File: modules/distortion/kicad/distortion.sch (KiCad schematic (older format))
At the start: 57 parts, among them P1 CONN_01X03, P10 CONN_01X03, P11 CONN_01X03, P12 CONN_01X03, P13 CONN_01X03, P14 CONN_01X03, P2 CONN_01X03, P3 CONN_01X03, P4 CONN_01X03, P5 CONN_01X03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

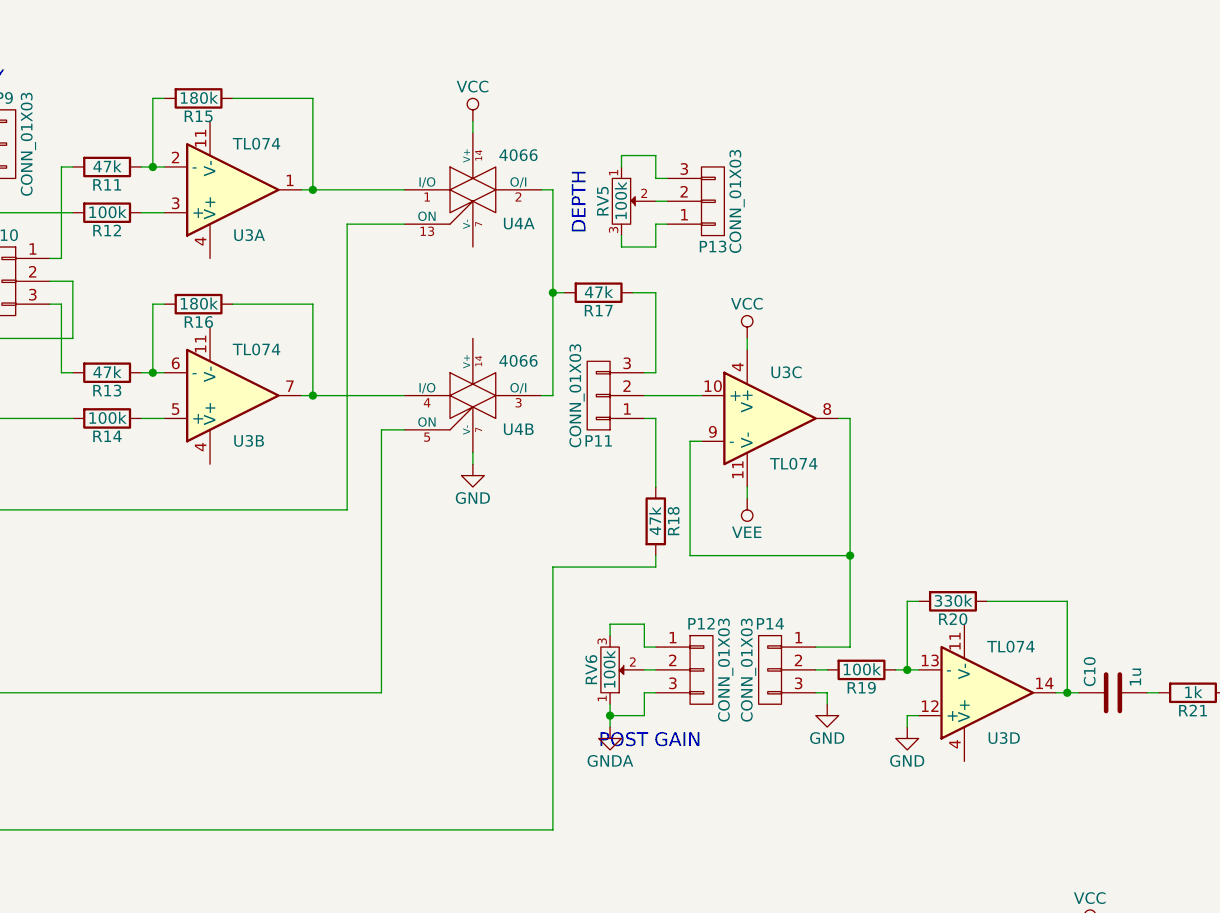
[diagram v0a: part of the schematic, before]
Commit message: Distortion pcb: panelization stuff, started layout wip
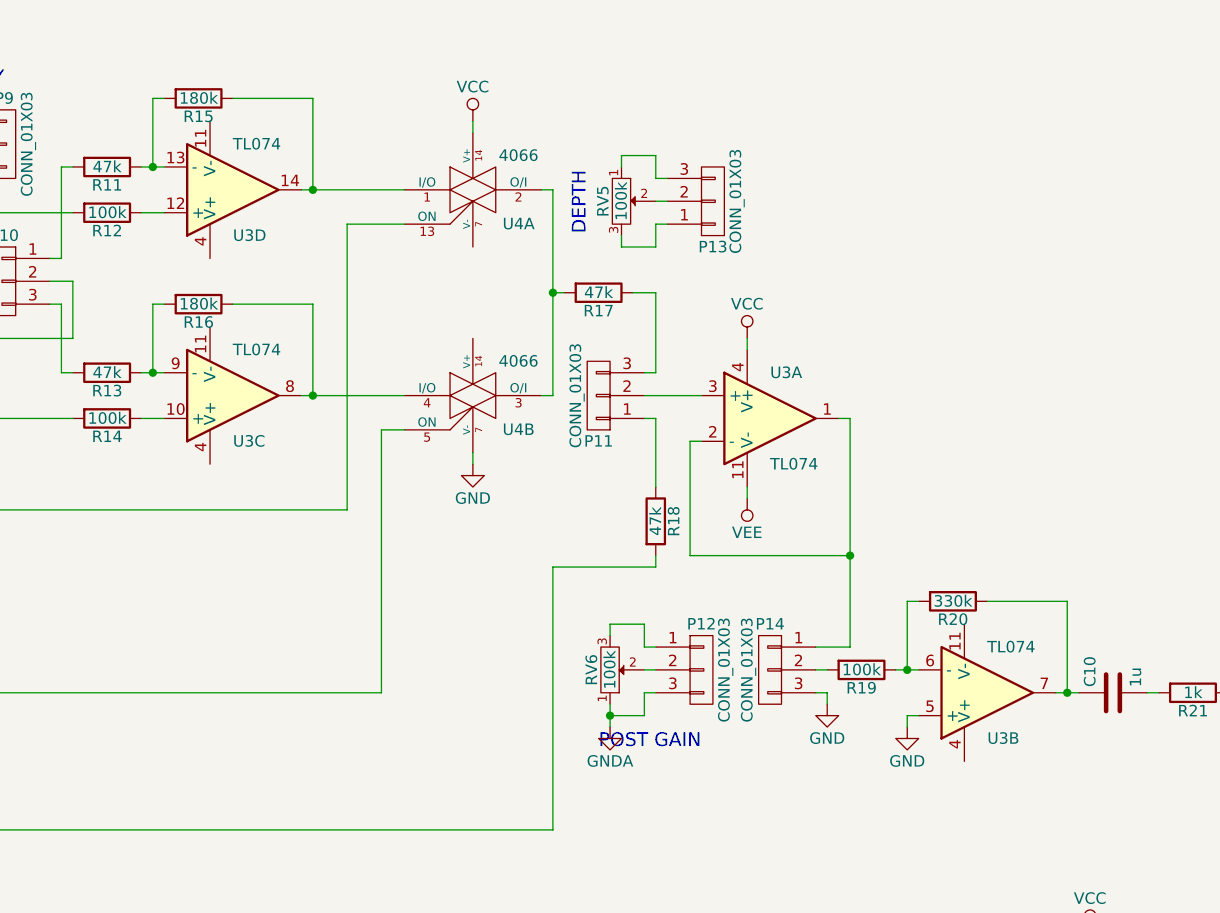
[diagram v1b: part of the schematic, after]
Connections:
- net GND: now also U3.5 (+); no longer U3.12 (+)
- net at R15.1, U4.1 (I/O): now also U3.14; no longer U3.1
- net at R11.1, R15.2: now also U3.13 (-); no longer U3.2 (-)
- net at R12.1: now also U3.12 (+); no longer U3.3 (+)
- net at P11.2 (P2): now also U3.3 (+); no longer U3.10 (+)
- net at R19.1, R20.2: now also U3.6 (-); no longer U3.13 (-)
- net at C10.1, R20.1: now also U3.7; no longer U3.14
- net at R14.1: now also U3.10 (+); no longer U3.5 (+)
- net at R13.1, R16.2: now also U3.9 (-); no longer U3.6 (-)
- net at R16.1, U4.4 (I/O): now also U3.8; no longer U3.7
- new net: P14.1 (P1), U3.1, U3.2 (-)
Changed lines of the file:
@@
 $Comp
 L TL074 U3
-U 1 1 597DDDFF
+U 4 1 597DDDFF
 P 5550 1400
 F 0 "U3" H 5550 1600 50  0000 L CNN
@@
 F 2 "Housings_DIP:DIP-14_W7.62mm_Socket_LongPads" H 5500 1500 50  0001 C CNN
 F 3 "" H 5600 1600 50  0000 C CNN
-	1    5550 1400
+	4    5550 1400
 	1    0    0    1
 $EndComp
 $Comp
 L TL074 U3
-U 3 1 597DDE8E
+U 1 1 597DDE8E
 P 7900 2400
 F 0 "U3" H 7900 2600 50  0000 L CNN
@@
 F 2 "Housings_DIP:DIP-14_W7.62mm_Socket_LongPads" H 7850 2500 50  0001 C CNN
 F 3 "" H 7950 2600 50  0000 C CNN
-	3    7900 2400
+	1    7900 2400
 	1    0    0    -1
 $EndComp
 $Comp
 L TL074 U3
-U 4 1 597DDEF7
+U 2 1 597DDEF7
 P 8850 3600
 F 0 "U3" H 8850 3800 50  0000 L CNN
@@
 F 2 "Housings_DIP:DIP-14_W7.62mm_Socket_LongPads" H 8800 3700 50  0001 C CNN
 F 3 "" H 8900 3800 50  0000 C CNN
-	4    8850 3600
+	2    8850 3600
 	1    0    0    1
 $EndComp
 $Comp
 L TL074 U3
-U 2 1 597DDF56
+U 3 1 597DDF56
 P 5550 2300
 F 0 "U3" H 5550 2500 50  0000 L CNN
@@
 F 2 "Housings_DIP:DIP-14_W7.62mm_Socket_LongPads" H 5500 2400 50  0001 C CNN
 F 3 "" H 5600 2500 50  0000 C CNN
-	2    5550 2300
+	3    5550 2300
 	1    0    0    1
 $EndComp
@@
 Connection ~ 7200 3700
 $Comp
-L GNDA #PWR?
+L GNDA #PWR032
 U 1 1 59875892
 P 3000 5650
-F 0 "#PWR?" H 3000 5400 50  0001 C CNN
+F 0 "#PWR032" H 3000 5400 50  0001 C CNN
 F 1 "GNDA" H 3000 5500 50  0000 C CNN
 F 2 "" H 3000 5650 50  0000 C CNN
@@
 $EndComp
 $Comp
-L PWR_FLAG #FLG?
+L PWR_FLAG #FLG033
 U 1 1 59876034
 P 3000 5600
-F 0 "#FLG?" H 3000 5695 50  0001 C CNN
+F 0 "#FLG033" H 3000 5695 50  0001 C CNN
 F 1 "PWR_FLAG" H 3000 5780 50  0000 C CNN
 F 2 "" H 3000 5600 50  0000 C CNN

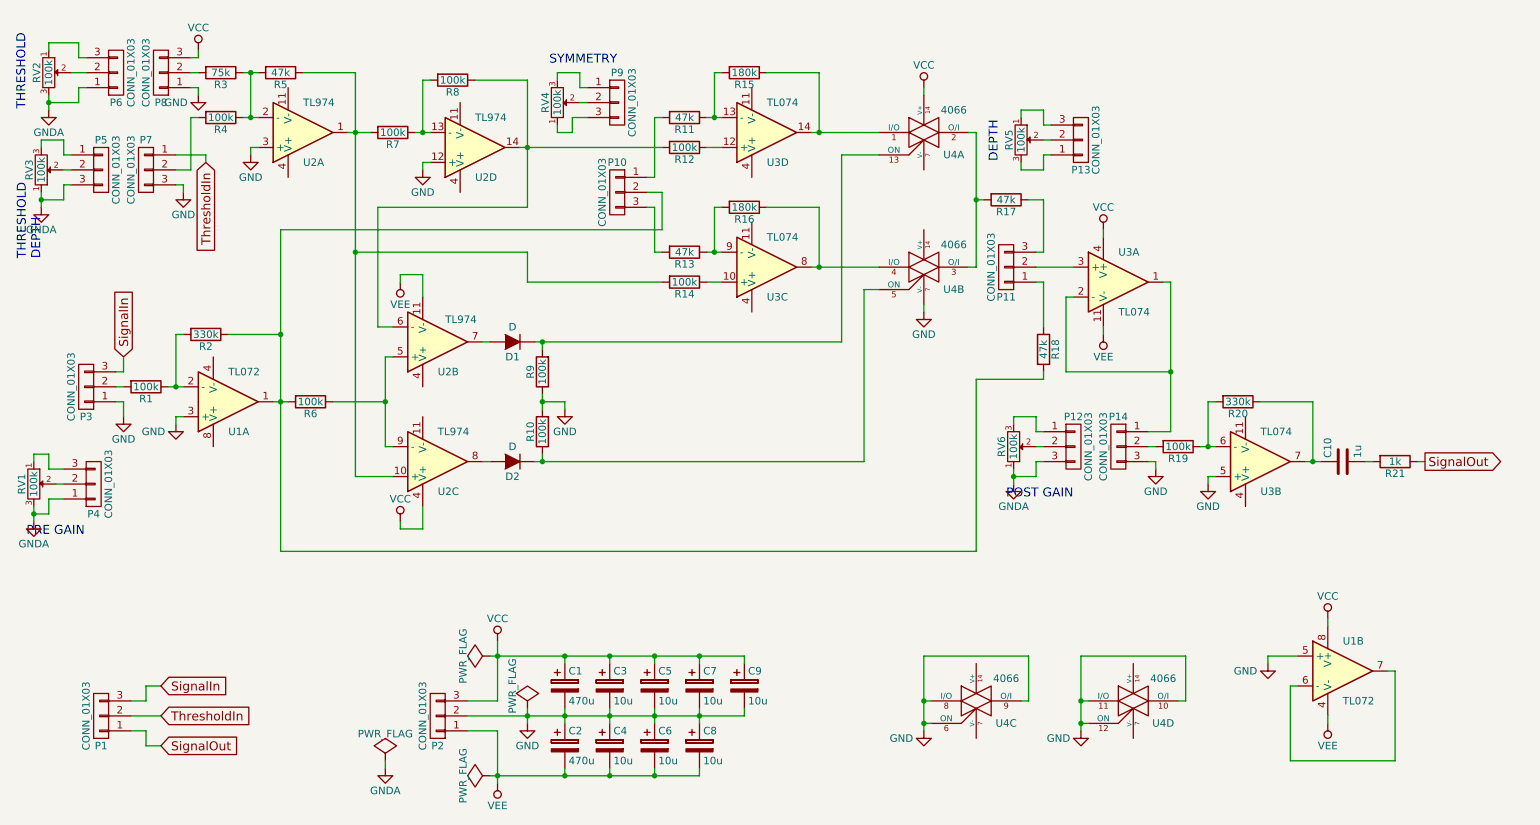
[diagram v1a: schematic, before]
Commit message: Distortion: move some resistors to top board WIP
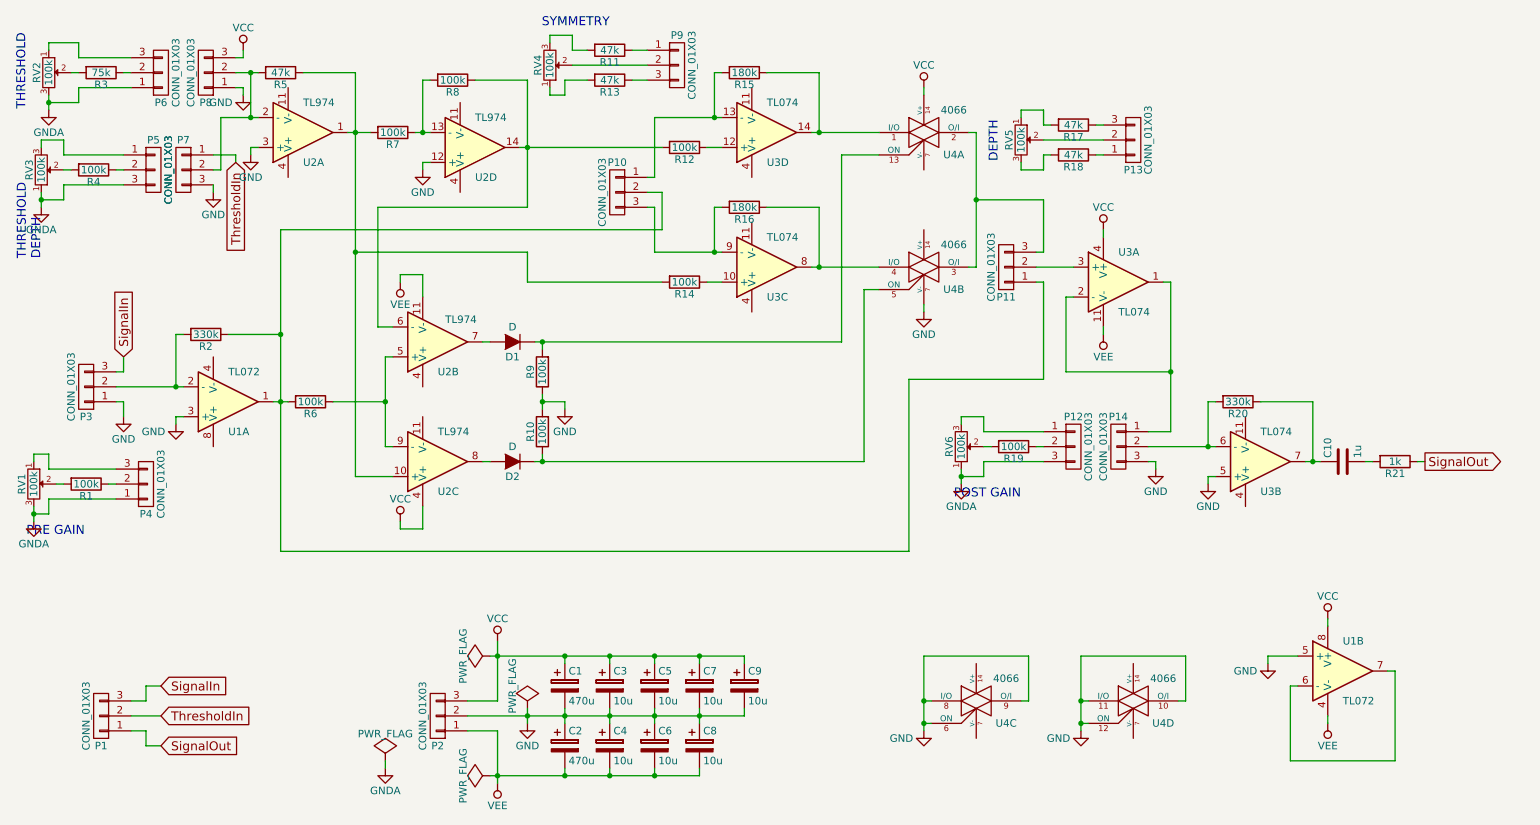
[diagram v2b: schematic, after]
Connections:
- net at R5.2, U2.2 (-): now also P7.2 (P2), P8.2 (P2); no longer R3.1, R4.1
- net at R15.2, U3.13 (-): now also P10.1 (P1); no longer R11.1
- net at R20.2, U3.6 (-): now also P14.2 (P2); no longer R19.1
- net at R16.2, U3.9 (-): now also P10.3 (P3); no longer R13.1
- net at U4.2 (O/I), U4.3 (O/I): now also P11.3 (P3); no longer R17.2
- net at RV2.2: now also R3.2; no longer P6.2 (P2)
- net at R4.2: now also RV3.2; no longer P7.2 (P2)
- net at P5.2 (P2): now also R4.1; no longer RV3.2
- net at P10.2 (P2), R2.1, R6.2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: now also P11.1 (P1); no longer R18.2
- net at R11.2: now also RV4.3; no longer P10.1 (P1)
- net at R13.2: now also RV4.1; no longer P10.3 (P3)
- net at P9.3 (P3): now also R13.1; no longer RV4.1
- net at P9.1 (P1): now also R11.1; no longer RV4.3
- net at R17.1: now also P13.3 (P3); no longer P11.3 (P3)
- net at R18.1: now also P13.1 (P1); no longer P11.1 (P1)
- net at RV5.1: now also R17.2; no longer P13.3 (P3)
- net at RV5.3: now also R18.2; no longer P13.1 (P1)
- net at RV6.2: now also R19.2; no longer P12.2 (P2)
- net at R2.2, U1.2 (-): now also P3.2 (P2); no longer R1.1
- net at R1.2: now also RV1.2; no longer P3.2 (P2)
- net at P4.2 (P2): now also R1.1; no longer RV1.2
- new net: P6.2 (P2), R3.1
- new net: P12.2 (P2), R19.1
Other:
- moved on the sheet: P13, P4, P5, P6, P7, P8, P9, R1, R11, R13, R17, R18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
